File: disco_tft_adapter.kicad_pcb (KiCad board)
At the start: 4 copper layers, 127 x 116.1 mm, 35 parts, among them J1 QTH-030-02-L-D-A, J2 F31L-1A7H1-11030

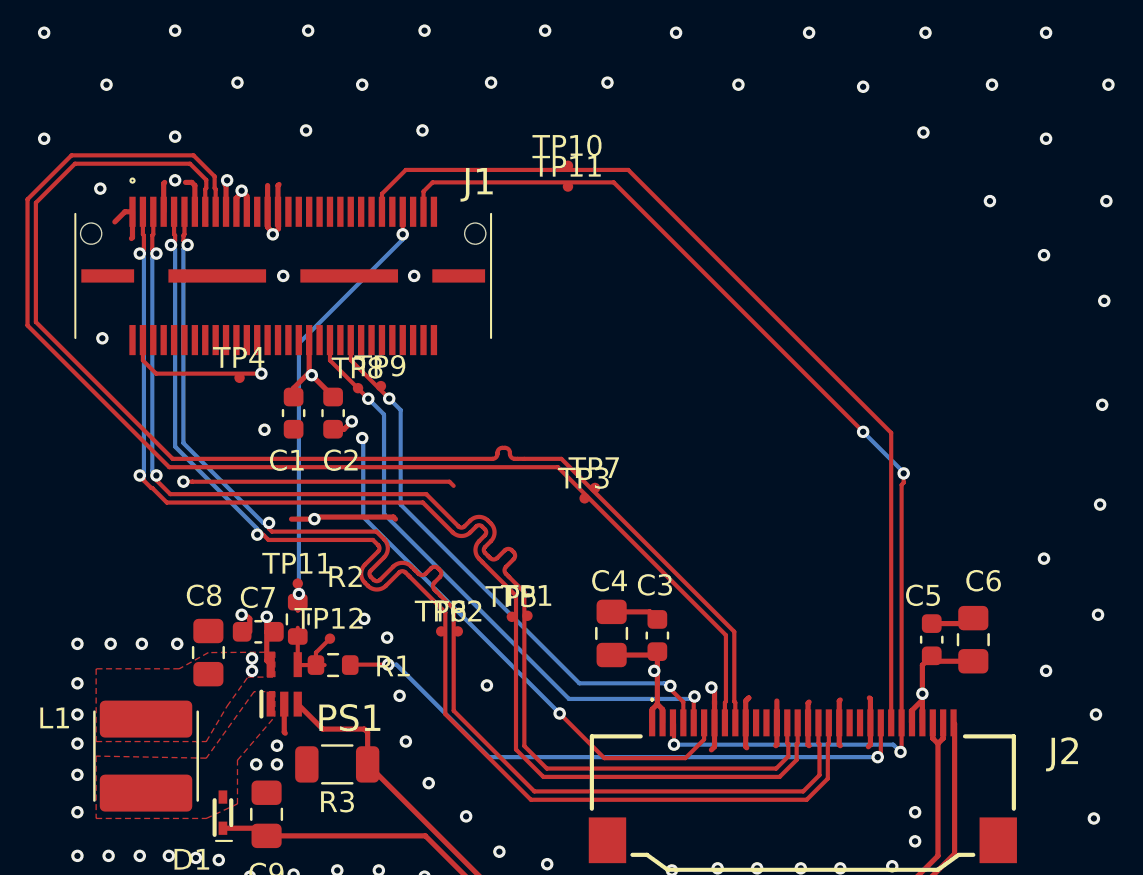
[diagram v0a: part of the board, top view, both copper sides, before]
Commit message: [layout] fixed DRC, added custom rule for J1
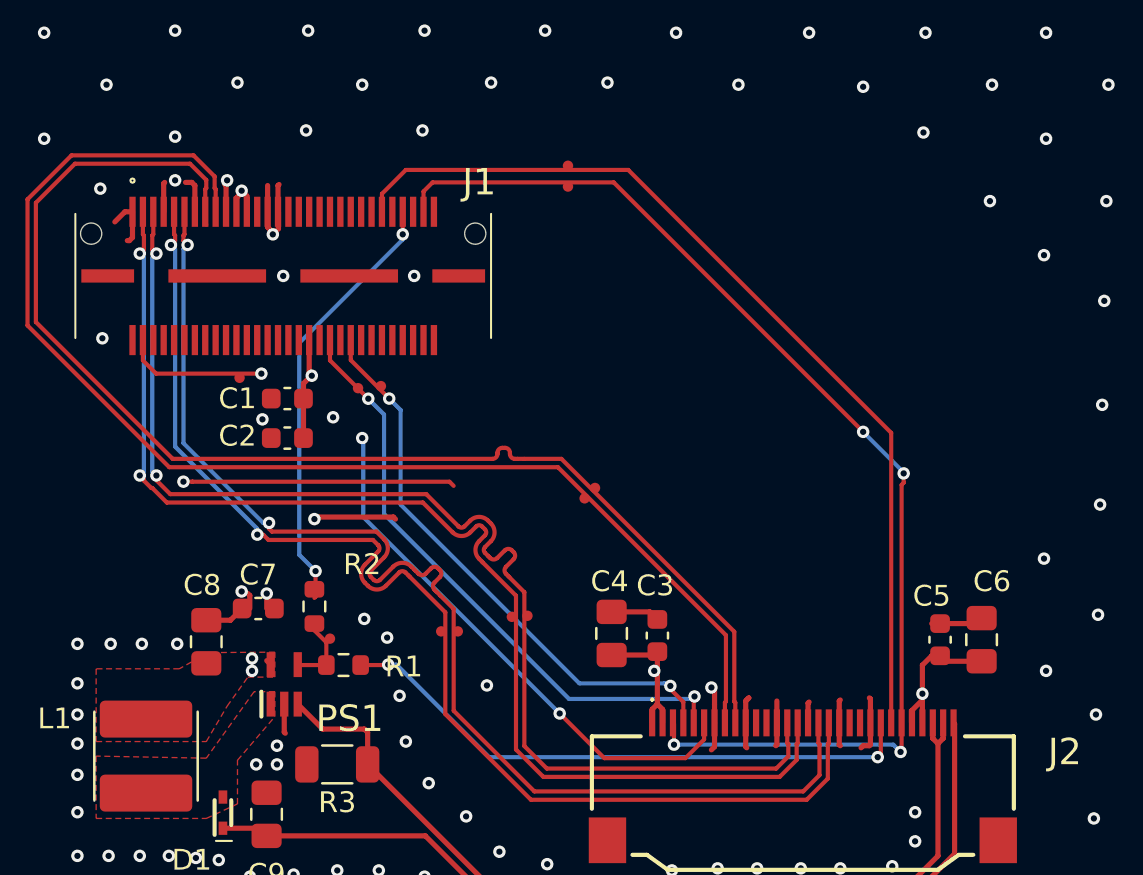
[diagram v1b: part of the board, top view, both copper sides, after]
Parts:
- removed the TP11 at (78.4, 110.4)
- moved C2 2.51 mm to (77.9, 103.4), turned to 180 degrees
- moved C7 1.12 mm to (76.5, 111.6)
- moved R2 1.01 mm to (79.2, 111.5)
- moved C1 0.76 mm to (77.9, 101.5), turned to 180 degrees
- moved C8 0.53 mm to (74.0, 113.2)
- moved R1 0.50 mm to (80.6, 114.3)
- moved C5 0.40 mm to (109.3, 113.1)
- moved C6 0.40 mm to (111.3, 113.1)
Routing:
- net VCC_BL: track 4.61 -> 3.23 mm
- net Net-(PS1-CTRL): track 4.62 -> 3.78 mm
- net GND: track 52.9 -> 52.2 mm
- net /PWM_DISP: track 28.9 -> 28.4 mm

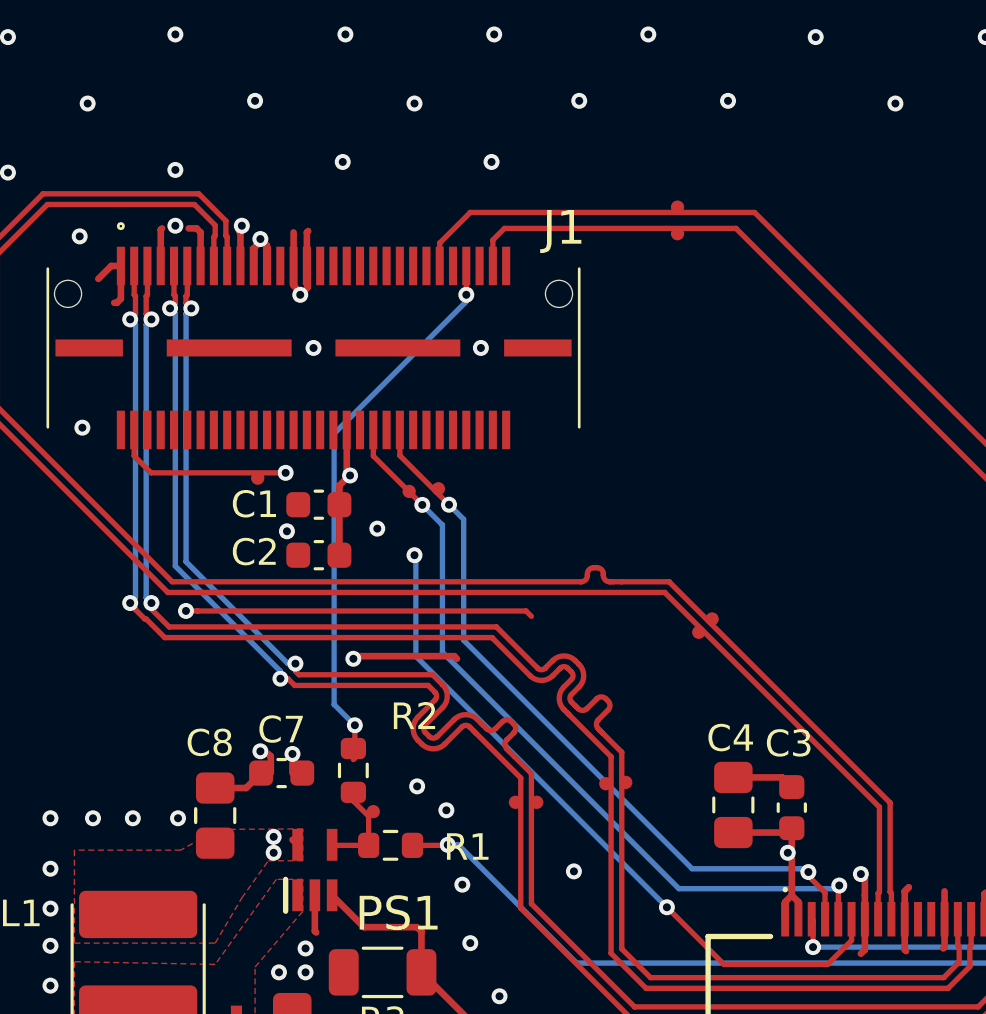
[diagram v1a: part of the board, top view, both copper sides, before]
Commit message: [layout] added labels for all test points
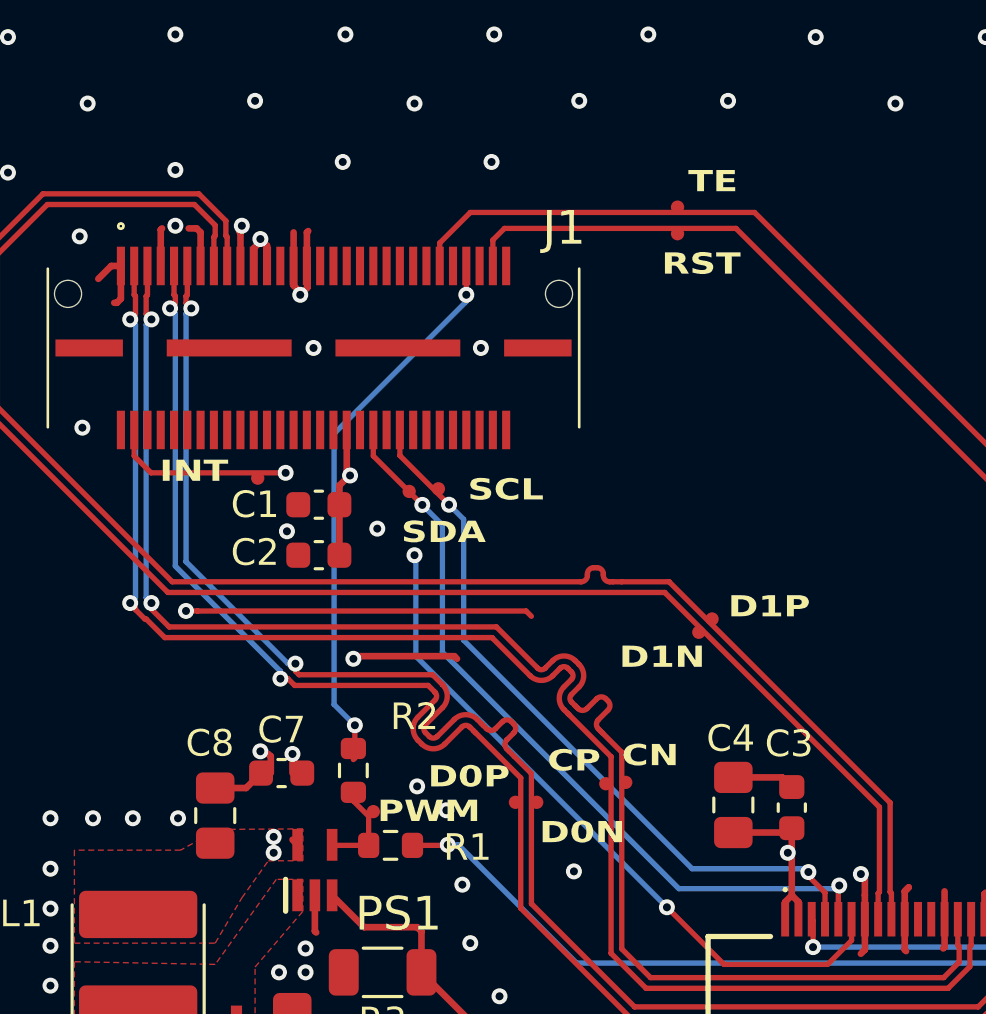
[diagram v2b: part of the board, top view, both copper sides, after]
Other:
- board text added: "CN"
- board text added: "CP"
- board text added: "D0N"
- board text added: "D0P"
- board text added: "D1N"
- board text added: "D1P"
- board text added: "INT"
- board text added: "PWM"
- board text added: "RST"
- board text added: "SCL"
- board text added: "SDA"
- board text added: "TE"
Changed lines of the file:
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@@
 		(layer "Edge.Cuts")
+	)
+	(gr_text "INT"
+		(at 71.9 100.7 0)
+		(layer "F.SilkS")
+		(effects
+			(font
+				(size 0.8 1)
+				(thickness 0.2)
+				(bold yes)
+			)
+			(justify left bottom)
+		)
+	)
+	(gr_text "PWM"
+		(at 80.1 113.5 0)
+		(layer "F.SilkS")
+		(effects
+			(font
+				(size 0.8 1)
+				(thickness 0.2)
+				(bold yes)
+			)
+			(justify left bottom)
+		)
+	)
+	(gr_text "SDA"
+		(at 81 103 0)
+		(layer "F.SilkS")
+		(effects
+			(font
+				(size 0.8 1)
+				(thickness 0.2)
+				(bold yes)
+			)
+			(justify left bottom)
+		)
+	)
+	(gr_text "D0P"
+		(at 82 112.2 0)
+		(layer "F.SilkS")
+		(effects
+			(font
+				(size 0.8 1)
+				(thickness 0.2)
+				(bold yes)
+			)
+			(justify left bottom)
+		)
+	)
+	(gr_text "SCL"
+		(at 83.5 101.4 0)
+		(layer "F.SilkS")
+		(effects
+			(font
+				(size 0.8 1)
+				(thickness 0.2)
+				(bold yes)
+			)
+			(justify left bottom)
+		)
+	)
+	(gr_text "D0N"
+		(at 86.2 114.3 0)
+		(layer "F.SilkS")
+		(effects
+			(font
+				(size 0.8 1)
+				(thickness 0.2)
+				(bold yes)
+			)
+			(justify left bottom)
+		)
+	)
+	(gr_text "CP"
+		(at 86.5 111.6 0)
+		(layer "F.SilkS")
+		(effects
+			(font
+				(size 0.8 1)
+				(thickness 0.2)
+				(bold yes)
+			)
+			(justify left bottom)
+		)
+	)
+	(gr_text "D1N"
+		(at 89.2 107.7 0)
+		(layer "F.SilkS")
+		(effects
+			(font
+				(size 0.8 1)
+				(thickness 0.2)
+				(bold yes)
+			)
+			(justify left bottom)
+		)
+	)
+	(gr_text "CN"
+		(at 89.3 111.4 0)
+		(layer "F.SilkS")
+		(effects
+			(font
+				(size 0.8 1)
+				(thickness 0.2)
+				(bold yes)
+			)
+			(justify left bottom)
+		)
+	)
+	(gr_text "RST"
+		(at 90.8 92.9 0)
+		(layer "F.SilkS")
+		(effects
+			(font
+				(size 0.8 1)
+				(thickness 0.2)
+				(bold yes)
+			)
+			(justify left bottom)
+		)
+	)
+	(gr_text "TE"
+		(at 91.8 89.8 0)
+		(layer "F.SilkS")
+		(effects
+			(font
+				(size 0.8 1)
+				(thickness 0.2)
+				(bold yes)
+			)
+			(justify left bottom)
+		)
+	)
+	(gr_text "D1P"
+		(at 93.3 105.8 0)
+		(layer "F.SilkS")
+		(effects
+			(font
+				(size 0.8 1)
+				(thickness 0.2)
+				(bold yes)
+			)
+			(justify left bottom)
+		)
 	)
 	(gr_text "Disco TFT Adapter\nRev. A"
